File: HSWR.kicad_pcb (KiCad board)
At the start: 4 copper layers, 152 x 220 mm, 221 parts, among them IC1 ADuM4160, IC2 ADM3054, IC3 B1212S-2W, IC4 JW5052C, J1 Motor1, J10 W2, J11 AVR-ISP-6, J12 ISP, J13 CAN, J14 Motor1, J15 FAN, J2 USB_B, J3 B+, J4 B-, J5 U1, J6 V1, J7 W1, J8 U2, J9 V2, Q1 Q_NMOS_GDS, Q10 IXFK300N20X3, Q11 IXFK300N20X3, Q12 IXFK300N20X3, Q13 IXFK300N20X3, Q2 IXFK300N20X3, Q3 IXFK300N20X3, Q4 IXFK300N20X3, Q5 IXFK300N20X3, Q6 IXFK300N20X3, Q7 IXFK300N20X3, Q8 IXFK300N20X3, Q9 IXFK300N20X3, U1 Opamp_Quad, U10 IRS2186, U11 IRS2186, U12 ACS781xLRTR-150B, U13 ACS781xLRTR-150B, U15 IRS2186, U16 IRS2186, U17 IRS2186, U18 Opamp_Quad, U19 ACS781xLRTR-150B, U2 AP1117-50, U20 ACS781xLRTR-150B, U3 ATtiny13A-SU, U5 ADuM120N, U6 ADuM261N, U8 STM32F405RGTx, U9 IRS2186, Y1 8MHz

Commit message: - layout almost finished
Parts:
- removed C23, C66: 1u, Capacitor_SMD:C_0805_2012Metric
- removed C33, C47, C67, C81: 100n, Capacitor_SMD:C_0805_2012Metric
- removed the C49 at (95.5, 247.8)
- removed the C59 at (57.8, 123.5)
- removed R11, R12: 0R, Resistor_SMD:R_0805_2012Metric
- removed the R3 at (178.8, 149.6)
- removed the R33 at (178.8, 142.8)
- removed the R34 at (178.8, 139.6)
- removed the R37 at (57.8, 113.0)
- removed the R4 at (178.8, 146.3)
- removed the REF** at (67.2, 123.0)
- removed the REF** at (115.2, 123.0)
- removed the U10 at (180.8, 223.3)
- removed the U11 at (189.8, 223.8)
- removed the U12 at (116.5, 224.0)
- removed the U13 at (74.2, 224.0)
- added NT1: Net-Tie_2, NetTie:NetTie-2_SMD_Pad2.0mm, F.Cu at (132.8, 123.0)
- C34, C48: moved to F.Cu
- U19, U20: moved to B.Cu
- moved C10 181.2 mm to (50.5, 111.5), turned to 90 degrees
- moved J12 165.5 mm to (73.0, 130.5), turned to -135 degrees
- moved L1 156.6 mm to (89.4, 111.1), turned to 45 degrees
- moved C1 155.4 mm to (86.0, 109.8)
- moved C21 155.4 mm to (72.8, 112.0), turned to 135 degrees
- moved R8 155.2 mm to (84.0, 109.8)
- moved C22 155.2 mm to (82.0, 109.8)
- moved C19 154.9 mm to (69.3, 121.8)
- moved C25 154.9 mm to (73.5, 124.8)
- moved D2 154.9 mm to (78.8, 130.3)
- moved D3 154.9 mm to (77.0, 130.3)
- moved D4 154.9 mm to (80.5, 130.3)
- moved R1 154.9 mm to (78.8, 127.1)
- moved R2 154.9 mm to (77.0, 127.1)
- moved R3 154.9 mm to (80.5, 127.1)
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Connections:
- net /Mosfet driver 1/U_GH renamed /Mosfet driver 1/U1_GH
- net /Mosfet driver 1/U_GL renamed /Mosfet driver 1/U1_GL
- net /Mosfet driver 1/U_VP renamed /Mosfet driver 1/U1_VP
- net /Mosfet driver 1/V_GH renamed /Mosfet driver 1/V1_GH
- net /Mosfet driver 1/V_GL renamed /Mosfet driver 1/V1_GL
- net /Mosfet driver 1/V_VP renamed /Mosfet driver 1/V1_VP
- net /Mosfet driver 1/W_GH renamed /Mosfet driver 1/W1_GH
- net /Mosfet driver 1/W_GL renamed /Mosfet driver 1/W1_GL
- net /Mosfet driver 2/U_GH renamed /Mosfet driver 2/U2_GH
- net /Mosfet driver 2/U_GL renamed /Mosfet driver 2/U2_GL
- net /Mosfet driver 2/U_VP renamed /Mosfet driver 2/U2_VP
- net /Mosfet driver 2/V_GH renamed /Mosfet driver 2/V2_GH
- net /Mosfet driver 2/V_GL renamed /Mosfet driver 2/V2_GL
- net /Mosfet driver 2/V_VP renamed /Mosfet driver 2/V2_VP
- net /Mosfet driver 2/W_GH renamed /Mosfet driver 2/W2_GH
- net /Mosfet driver 2/W_GL renamed /Mosfet driver 2/W2_GL
- net /Power MOSFETS 1/U renamed /Power MOSFETS 1/U1
- net /Power MOSFETS 1/V renamed /Power MOSFETS 1/V1
- net /Power MOSFETS 2/U renamed /U2
- net /Power MOSFETS 2/V renamed /V2
- C31 pad 2: /Mosfet driver 1/W_VP -> /Mosfet driver 1/W1_VP
- C49 pad 1: /Power MOSFETS 1/V_I -> /MCU/W1_I
- C65 pad 2: /Mosfet driver 2/W_VP -> /W2
- C83 pad 1: /Power MOSFETS 2/V_I -> /MCU/W2_I
- J10 pad 1: /W -> /W2
- J7 pad 1: /W_1 -> /Mosfet driver 1/W1_VP
- Q12 pad 3: /Mosfet driver 2/W_VP -> /W2
- Q13 pad 2: /Mosfet driver 2/W_VP -> /W2
- Q6 pad 3: /Mosfet driver 1/W_VP -> /Mosfet driver 1/W1_VP
- Q7 pad 2: /Mosfet driver 1/W_VP -> /Mosfet driver 1/W1_VP
- R37 pad 2: /Mosfet driver 1/W_VP -> /Mosfet driver 1/W1_VP
- R43 pad 1: /Power MOSFETS 1/V_I -> /MCU/W1_I
- R58 pad 2: /Mosfet driver 2/W_VP -> /W2
- R64 pad 1: /Power MOSFETS 2/V_I -> /MCU/W2_I
- U11 pad 6: /Mosfet driver 1/W_VP -> /Mosfet driver 1/W1_VP
- U17 pad 6: /Mosfet driver 2/W_VP -> /W2
- U18 pad 12: (no net) -> GND
- U18 pad 13: (no net) -> Net-(U18D--)
- U18 pad 14: (no net) -> Net-(U18D--)
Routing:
- net +3V3: track 14.1 -> 381.0 mm, vias 4 -> 15
- net GND: track 8.76 -> 308.1 mm, vias 4 -> 9
- net /Mosfet driver 1/W1_VP: track 0.00 -> 232.8 mm, vias 0 -> 4
- net /W2: track 0.00 -> 215.8 mm, vias 0 -> 2
- net /Mosfet driver 2/V2_VP: track 0.00 -> 169.8 mm, vias 0 -> 22
- net /Mosfet driver 2/U2_VP: track 0.00 -> 161.5 mm, vias 0 -> 22
- net /Mosfet driver 1/U1_VP: track 30.4 -> 165.7 mm, vias 15 -> 22
- net /Mosfet driver 1/V1_VP: track 29.0 -> 161.5 mm, vias 30 -> 23
- net /Mosfet driver 2/W2_GH: track 0.00 -> 97.4 mm, vias 0 -> 2
- net /Mosfet driver 1/U1_GH: track 1.31 -> 96.1 mm, vias 1 -> 2
- net /Mosfet driver 2/U2_GL: track 0.00 -> 84.8 mm, vias 0 -> 2
- net /Mosfet driver 2/W2_GL: track 0.00 -> 82.7 mm, vias 0 -> 2
- net /Mosfet driver 1/V1_GH: track 1.06 -> 82.8 mm, vias 1 -> 2
- net Net-(U19-VOUT): track 0.00 -> 80.2 mm, vias 0 -> 2
- net /Mosfet driver 2/V2_GH: track 0.00 -> 79.7 mm, vias 0 -> 2
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- added copper zone on B.Cu, net /Mosfet driver 1/W1_VP
- added copper zone on F.Cu, net /Mosfet driver 1/W1_VP
- added copper zone on In1.Cu, net /Mosfet driver 1/W1_VP
- added copper zone on In2.Cu, net /Mosfet driver 1/W1_VP
- added copper zone on B.Cu, net /Mosfet driver 2/U2_VP
- added copper zone on F.Cu, net /Mosfet driver 2/U2_VP
- added copper zone on In1.Cu, net /Mosfet driver 2/U2_VP
- added copper zone on In2.Cu, net /Mosfet driver 2/U2_VP
- added copper zone on B.Cu, net /Mosfet driver 2/V2_VP
- added copper zone on F.Cu, net /Mosfet driver 2/V2_VP
- added copper zone on In1.Cu, net /Mosfet driver 2/V2_VP
- added copper zone on In2.Cu, net /Mosfet driver 2/V2_VP
- added copper zone on B.Cu, net /W2
- added copper zone on F.Cu, net /W2
- added copper zone on In1.Cu, net /W2
- added copper zone on In2.Cu, net /W2
- removed copper zone on B.Cu, net /Mosfet driver 1/W_VP
- removed copper zone on F.Cu, net /Mosfet driver 1/W_VP
- removed copper zone on In1.Cu, net /Mosfet driver 1/W_VP
- removed copper zone on In2.Cu, net /Mosfet driver 1/W_VP
- removed copper zone on In1.Cu, net GND
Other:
- board text added: "HSWR DUAL V1 200V+ 100A *20231116 Schröder Planung & Entwicklung"
- board text added: "MOTOR1"
- board text added: "MOTOR2"
- board text removed: "GND Fan- Fan+ MT UB UA H3B H3A H2B H2A H1B H1A GND CanL CanH VCC"
- board text removed: "HSWR V4.1 200V+ 100A *20231116 Alexander Schröder"

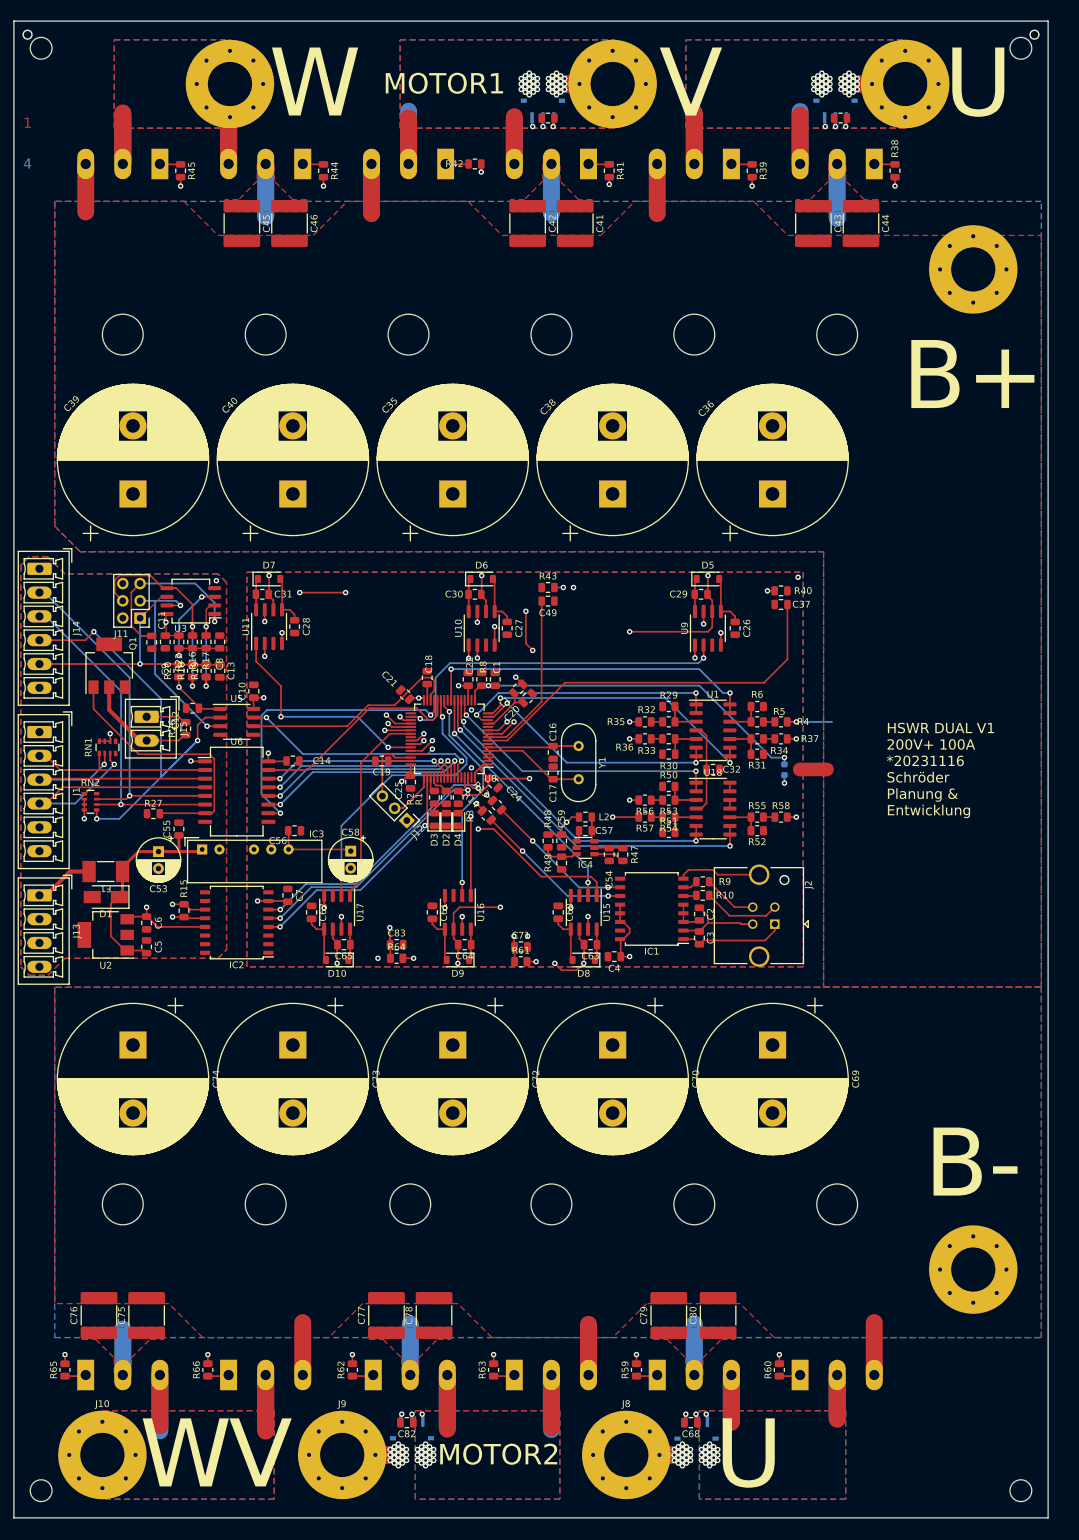
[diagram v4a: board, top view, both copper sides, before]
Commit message: - peeled back the flood fill - improved insulation on HV logic - checked all labels on silk screen - added pinouts for connectors - last fixes before export
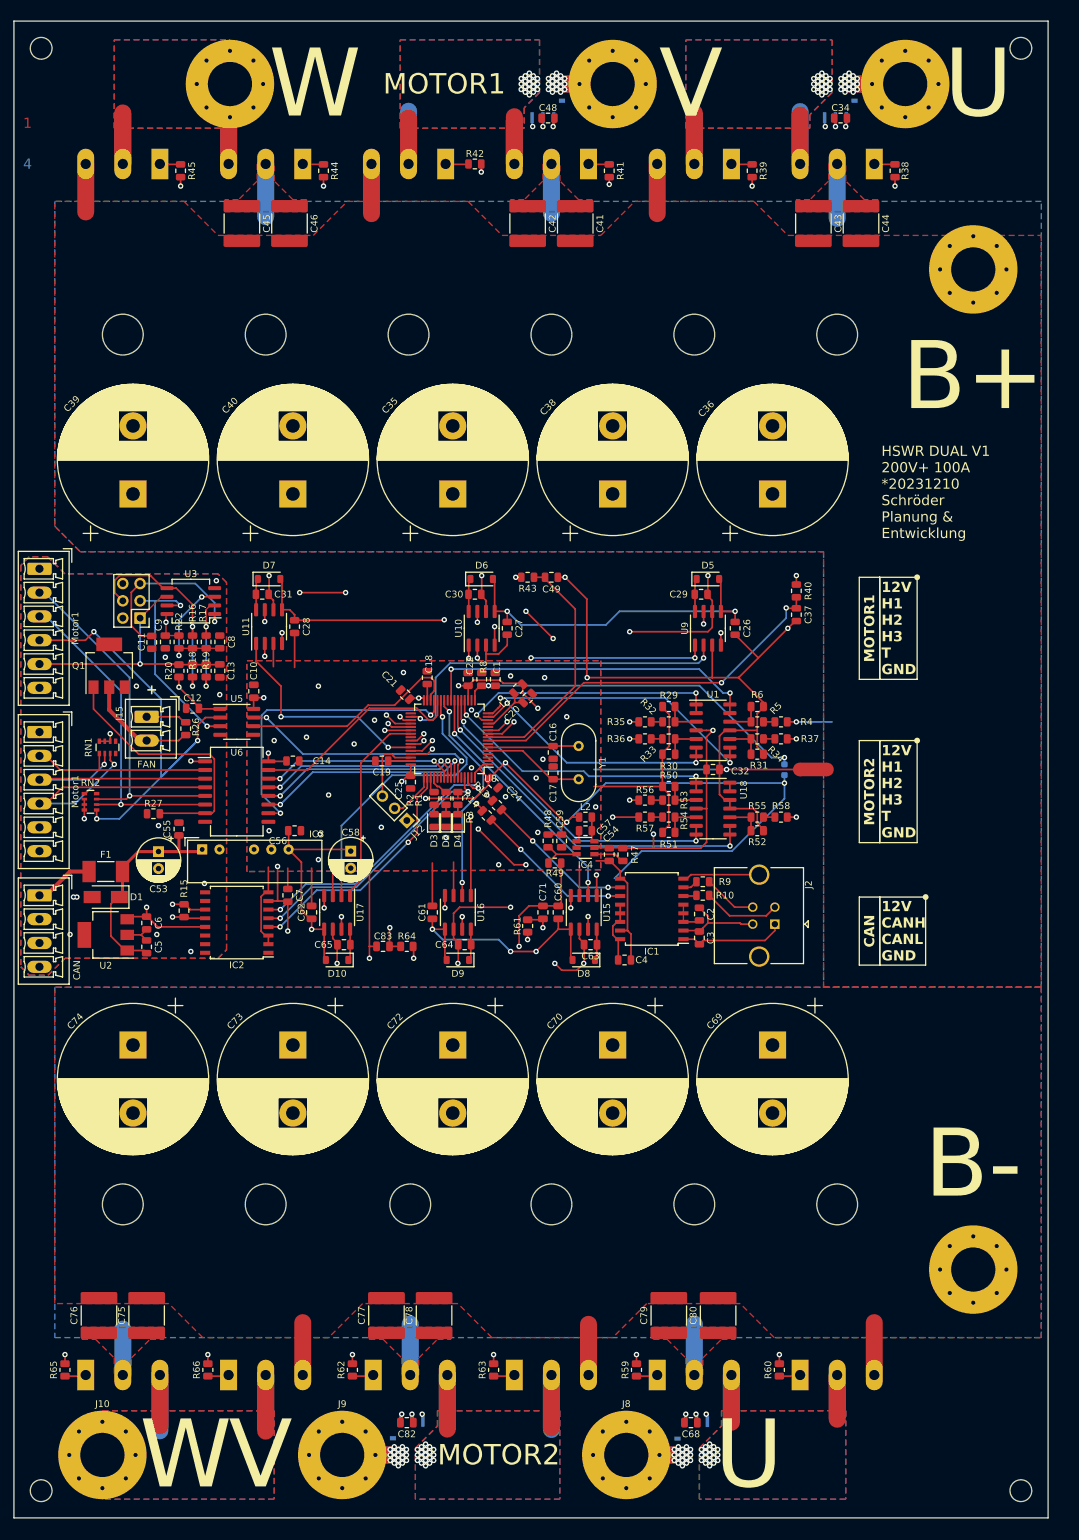
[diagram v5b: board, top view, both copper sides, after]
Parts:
- moved C71 6.02 mm to (93.0, 144.0), turned to 90 degrees
- moved R61 5.34 mm to (90.8, 146.0), turned to -90 degrees
- moved C49 3.54 mm to (94.2, 94.8)
- moved R43 3.35 mm to (90.8, 94.8), turned to 180 degrees
- moved C37 2.70 mm to (130.2, 100.2), turned to -90 degrees
- moved R64 2.30 mm to (73.0, 149.0)
- moved R40 2.25 mm to (130.2, 96.8), turned to 90 degrees
- moved C83 2.02 mm to (69.5, 149.0), turned to 180 degrees
- moved C4 1.58 mm to (105.0, 151.0), turned to 180 degrees
- moved R49 1.00 mm to (94.8, 136.8), turned to 0 degrees
- moved D2 0.16 mm to (78.8, 130.5)
- moved D3 0.16 mm to (77.0, 130.5)
- moved D4 0.16 mm to (80.5, 130.5)
- moved R1 0.16 mm to (78.8, 127.2)
- moved R2 0.16 mm to (77.0, 127.2)
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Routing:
- net GND: track 308.1 -> 582.2 mm, vias 9 -> 32
- net +12V: track 76.1 -> 274.9 mm, vias 0 -> 9
- net +3V3: track 381.0 -> 549.3 mm, vias 15 -> 17
- net /MCU/W1_I: track 24.8 -> 35.4 mm
- net Net-(U13-VOUT): track 74.5 -> 69.4 mm
- net Earth: track 0.00 -> 4.34 mm, vias 1 -> 11
- net Net-(U12-VOUT): track 74.2 -> 70.4 mm
- net Net-(U19-VOUT): track 80.2 -> 83.7 mm
- net Net-(IC4-FB): track 4.79 -> 6.29 mm
- net Net-(D4-A): track 0.00 -> 1.38 mm
- net Net-(D3-A): track 0.00 -> 1.38 mm
- net Net-(D2-A): track 0.00 -> 1.38 mm
- net /MCU/V1_PWM_L: track 18.6 -> 20.0 mm
- net /MCU/U1_I: track 57.0 -> 55.9 mm, vias 0 -> 2
- net GNDD: track 40.2 -> 39.3 mm
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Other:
- rule pad_to_mask_clearance: 0.1 -> 0
- board text added: "+"
- board text added: "12V CANH CANL GND"
- board text added: "12V H1 H2 H3 T GND"
- board text added: "CAN"
- board text added: "HSWR DUAL V1 200V+ 100A *20231210 Schröder Planung & Entwicklung"
- board text removed: "HSWR DUAL V1 200V+ 100A *20231116 Schröder Planung & Entwicklung"
